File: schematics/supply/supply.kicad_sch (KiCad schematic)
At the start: 14 parts, among them J1 Conn_01x02_Pin, J2 Conn_01x02_Pin, J3 Conn_01x01_Pin, J4 Conn_01x01_Pin

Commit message: Project splited to 2 sub-projects - I want to reduce board production price
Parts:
- removed H1 (x3): MountingHole, MountingHole:MountingHole_2.2mm_M2, symbol Mechanical:MountingHole
- removed J1: Conn_01x02_Pin, Connector_Wire:SolderWire-1.5sqmm_1x02_P6mm_D1.7mm_OD3mm, symbol Connector:Conn_01x02_Pin
- removed J3: Conn_01x01_Pin, Connector_Wire:SolderWire-1.5sqmm_1x01_D1.7mm_OD3.9mm, symbol Connector:Conn_01x01_Pin
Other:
- removed sheet Input power with filter
- removed sheet Standby Supply
- note removed: "Holes on board#2"
- moved on the sheet: J2, J4

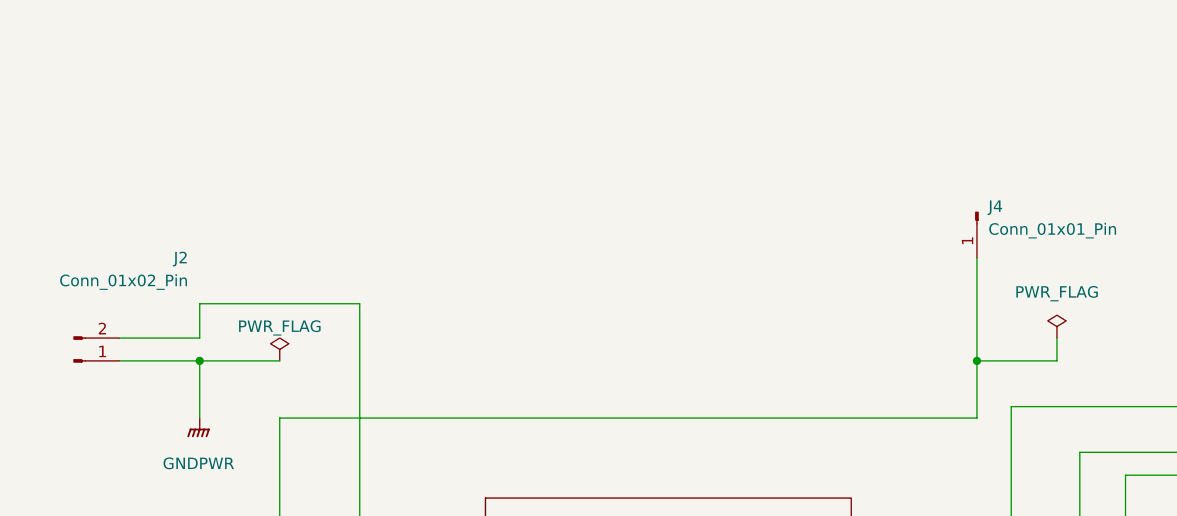
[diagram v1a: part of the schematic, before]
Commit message: UV board size changed to 100x100 to reduce production price
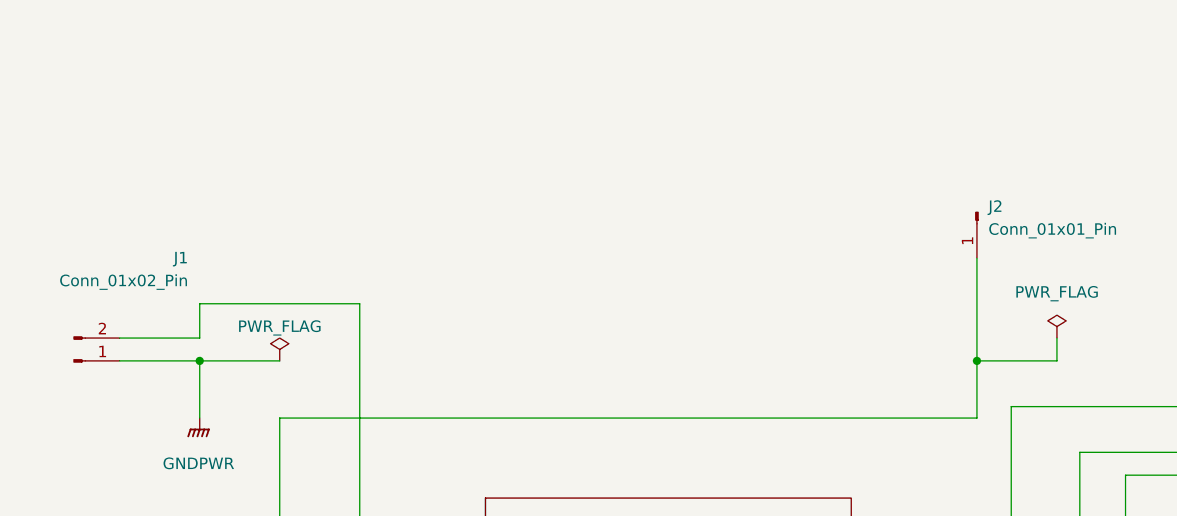
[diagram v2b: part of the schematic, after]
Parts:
- renumbered J2 to J1, J4 to J2
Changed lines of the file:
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@@
   (symbol (lib_id "Connector:Conn_01x01_Pin") (at 157.48 52.07 270) (unit 1)
     (in_bom yes) (on_board yes) (dnp no) (fields_autoplaced)
-    (property "Reference" "J4" (at 158.75 51.435 90)
+    (property "Reference" "J2" (at 158.75 51.435 90)
       (effects (font (size 1.27 1.27)) (justify left))
     )
@@
       (project "supply"
         (path "/1e139717-fcd1-4008-a6ea-4c993845e928"
-          (reference "J4") (unit 1)
+          (reference "J2") (unit 1)
         )
       )
@@
   (symbol (lib_id "Connector:Conn_01x02_Pin") (at 57.15 68.58 0) (mirror x) (unit 1)
     (in_bom yes) (on_board yes) (dnp no)
-    (property "Reference" "J2" (at 69.85 57.15 0)
+    (property "Reference" "J1" (at 69.85 57.15 0)
       (effects (font (size 1.27 1.27)) (justify right))
     )
@@
       (project "supply"
         (path "/1e139717-fcd1-4008-a6ea-4c993845e928"
-          (reference "J2") (unit 1)
+          (reference "J1") (unit 1)
         )
       )

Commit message: Found and fixed issues in schematics.
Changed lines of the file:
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@@
     (stroke (width 0) (type default))
+  )
+  (text_box "Known issues:\n1. Wrong symbol for protection diodes SMAJxx, be carefull with soldering!"
+    (at 314.96 17.78 0) (size 83.82 59.69)
+    (stroke (width 0) (type default))
+    (fill (type none))
+    (effects (font (size 1.27 1.27)) (justify left top))
   )
   (text_box "Startup sequence:\n1. UV board\n1.0 check resistance on 220V connector, OUT_400V connector and STB VCC connector\n1.1 connect 220V\n1.2 check: \n    - OUT_400V is a 310V\n    - PFC EN jumper has 13.7V on one side \n    - STB EN is a HIGH on one side\n    - STB VCC has no power\n    - relay is OFF\n    - LED PFCRDY is ON\n    - LED STBOK is OFF\n1.3 solder PFC EN jumoer\n1.4 check:\n    - OUT_400V is a 400V\n    - PFC EN jumper has 13.7V\n    - STB EN is a LOW on one side\n    - STB VCC has no power\n    - relay is ON\n    - LED PFCRDY is ON\n    - LED STBOK is OFF\n1.5 solder STB EN\n1.6 check:\n    - OUT_400V is a 400V\n    - PFC EN jumper has 13.7V\n    - STB EN is a LOW\n    - STB VCC has 13.7V\n    - relay is ON\n    - LED PFCRDY is ON\n    - LED STBOK is ON\n\n2. UV board & power boards\n2.1 check resistance on +400V connector, PWR OUT connector, 5V connector 3.3V connector and all jumpers\n2.2 flush firmwares\n2.3 connect VV board to power board and connect 220V\n2.4 check:\n    - +400V has 400V\n    - STB VCC has 13.7V\n    - PWR OUT has now power\n    - +5V and 3.3V connectors power\n    - USBx jumper and +5V SYS jumper has 5V on one side\n2.5 insert +5V SYS fuse\n2.6 check:\n    - +5V and 3.3V connectors has no power\n    - USBx jumper has 5V on one side\n    - +5V SYS has 5V\n    - Display is ON\n    - PWR OUT voltage controlled by chips\n    - FAN controlled by termisters and chip\n2.7 solder USB2 & USB3 jumpers\n2.8 check: \n    - usb2 & usb3 works\n    - usb2 & usb3 leds works\n    - display shows usb2 & usb3 voltage and current\n2.9 solder USB1 jumper\n2.10 check \n    - usb1 works\n    - usb1 QC works\n    - usb1 led works\n    - display shows usb1 voltage and current\n"

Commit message: Continue soldering and setting up hardware
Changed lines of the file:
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@@
     (stroke (width 0) (type default))
   )
-  (text_box "Known issues:\n1. Wrong symbol for protection diodes SMAJxx, be carefull with soldering!"
+  (text_box "Known issues:\n1. Wrong symbol for protection diodes SMAJxx, be carefull with soldering!\n2. Power output starts without +5VSYS"
     (at 314.96 17.78 0) (size 83.82 59.69)
     (stroke (width 0) (type default))

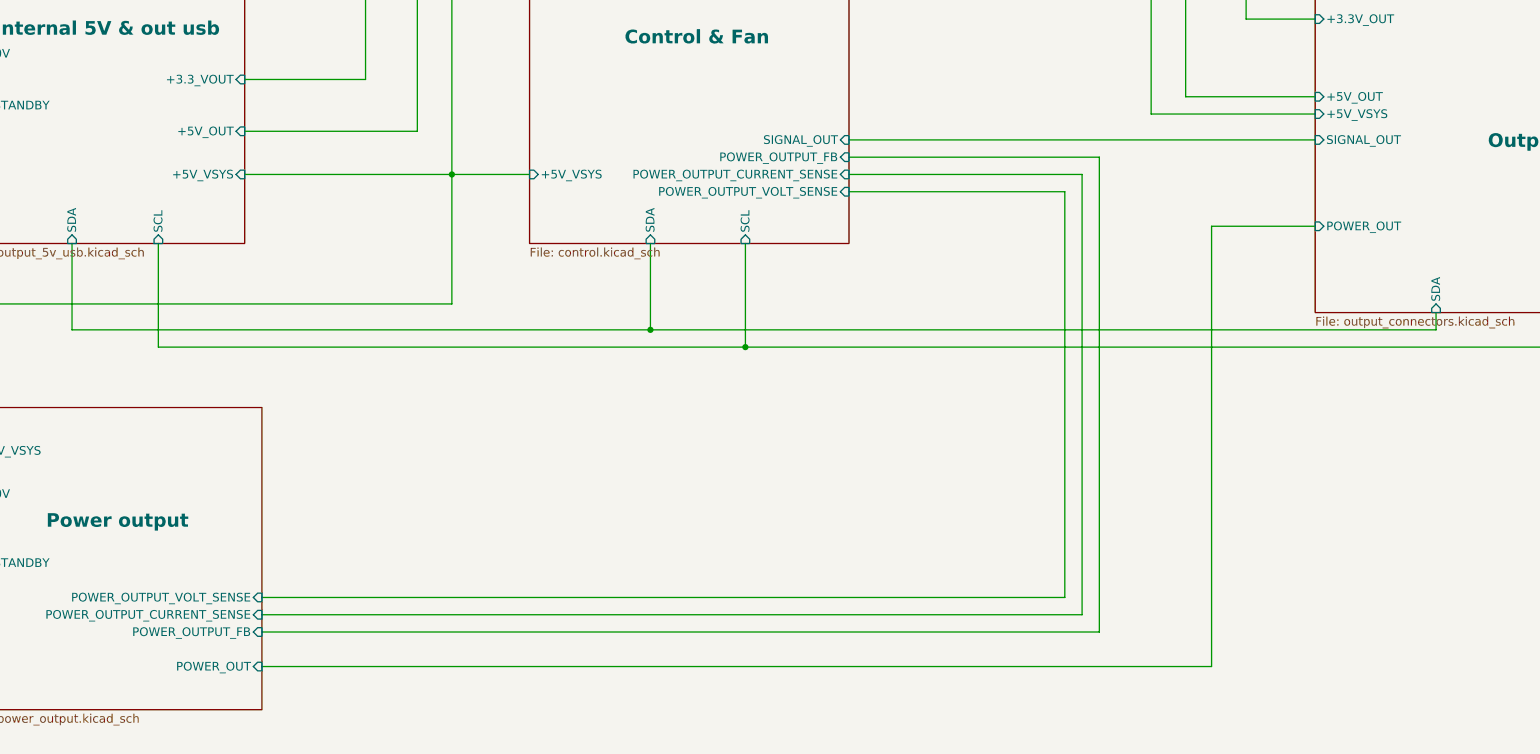
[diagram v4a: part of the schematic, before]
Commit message: supply board - power controllers changed; PWM logic changed
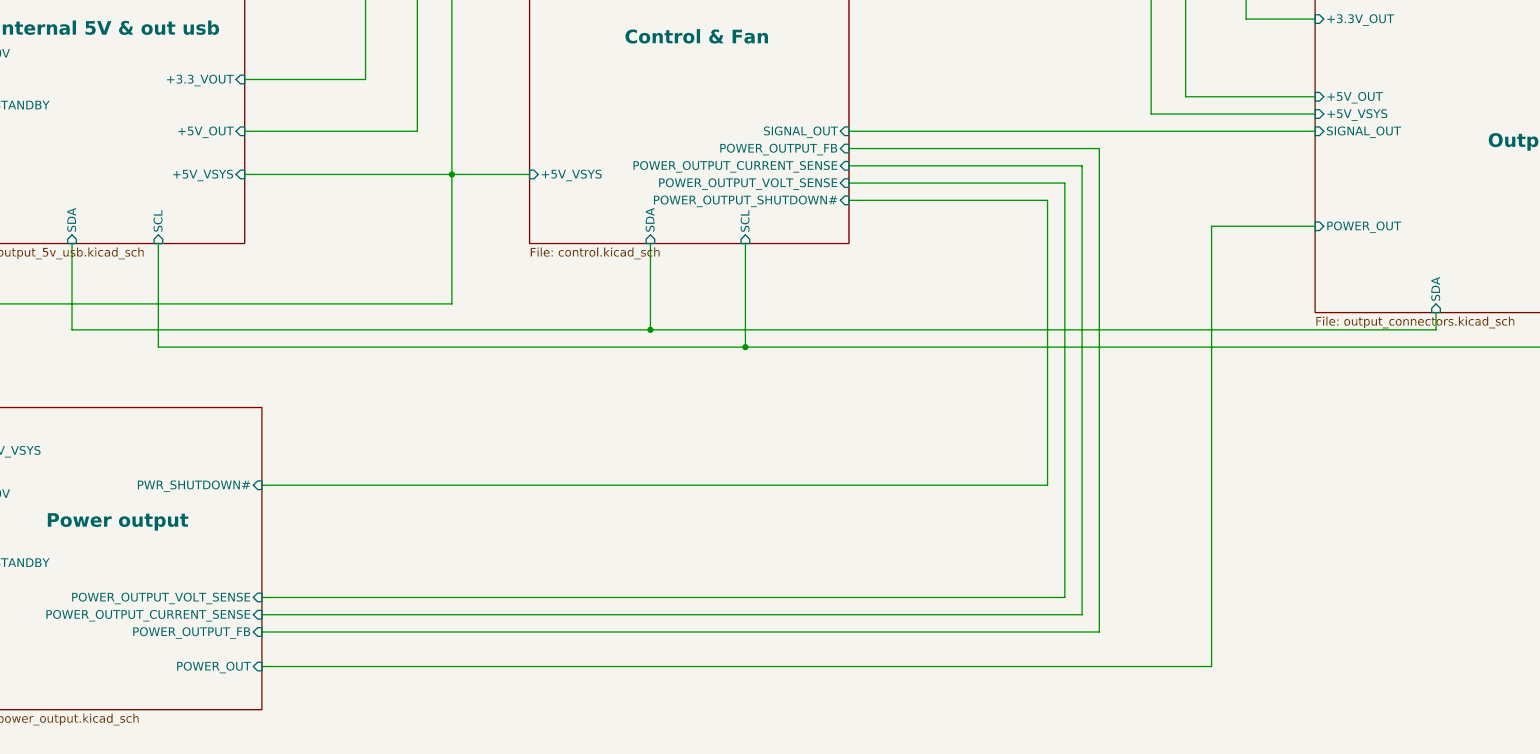
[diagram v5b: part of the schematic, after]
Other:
- sheet Control & Fan ports: added POWER_OUTPUT_SHUTDOWN#; removed none
- sheet Power output ports: added PWR_SHUTDOWN#; removed none
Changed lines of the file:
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@@
     (stroke (width 0) (type default))
   )
-  (wire (pts (xy 269.24 111.76) (xy 232.41 111.76))
+  (wire (pts (xy 269.24 110.49) (xy 232.41 110.49))
     (stroke (width 0) (type default))
   )
@@
     (stroke (width 0) (type default))
   )
+  (wire (pts (xy 261.62 160.02) (xy 146.05 160.02))
+    (stroke (width 0) (type default))
+  )
   (wire (pts (xy 166.37 68.58) (xy 157.48 68.58))
     (stroke (width 0) (type default))
   )
-  (wire (pts (xy 269.24 181.61) (xy 269.24 111.76))
+  (wire (pts (xy 269.24 181.61) (xy 269.24 110.49))
+    (stroke (width 0) (type default))
+  )
+  (wire (pts (xy 232.41 107.95) (xy 300.99 107.95))
     (stroke (width 0) (type default))
   )
@@
     (stroke (width 0) (type default))
   )
-  (wire (pts (xy 266.7 114.3) (xy 266.7 179.07))
+  (wire (pts (xy 266.7 113.03) (xy 266.7 179.07))
     (stroke (width 0) (type default))
   )
@@
     (stroke (width 0) (type default))
   )
-  (wire (pts (xy 232.41 109.22) (xy 300.99 109.22))
-    (stroke (width 0) (type default))
-  )
   (wire (pts (xy 71.12 68.58) (xy 80.01 68.58))
     (stroke (width 0) (type default))
@@
     (stroke (width 0) (type default))
   )
+  (wire (pts (xy 261.62 118.11) (xy 261.62 160.02))
+    (stroke (width 0) (type default))
+  )
   (wire (pts (xy 88.9 96.52) (xy 88.9 62.23))
     (stroke (width 0) (type default))
@@
     (stroke (width 0) (type default))
   )
-  (wire (pts (xy 264.16 116.84) (xy 232.41 116.84))
+  (wire (pts (xy 264.16 115.57) (xy 232.41 115.57))
     (stroke (width 0) (type default))
   )
@@
     (stroke (width 0) (type default))
   )
-  (wire (pts (xy 264.16 176.53) (xy 264.16 116.84))
-    (stroke (width 0) (type default))
-  )
-  (wire (pts (xy 232.41 114.3) (xy 266.7 114.3))
+  (wire (pts (xy 264.16 176.53) (xy 264.16 115.57))
+    (stroke (width 0) (type default))
+  )
+  (wire (pts (xy 232.41 113.03) (xy 266.7 113.03))
     (stroke (width 0) (type default))
   )
@@
   )
   (wire (pts (xy 161.29 100.33) (xy 161.29 73.66))
+    (stroke (width 0) (type default))
+  )
+  (wire (pts (xy 232.41 118.11) (xy 261.62 118.11))
     (stroke (width 0) (type default))
   )
@@
       (effects (font (size 1.27 1.27)) (justify left))
     )
-    (pin "SIGNAL_OUT" input (at 300.99 109.22 180)
+    (pin "SIGNAL_OUT" input (at 300.99 107.95 180)
       (effects (font (size 1.27 1.27)) (justify left))
     )
@@
       (effects (font (size 1.27 1.27)) (justify left))
     )
+    (pin "PWR_SHUTDOWN#" input (at 146.05 160.02 0)
+      (effects (font (size 1.27 1.27)) (justify right))
+    )
     (instances
       (project "supply"
@@
       (effects (font (size 1.27 1.27)) (justify left))
     )
-    (pin "SIGNAL_OUT" input (at 232.41 109.22 0)
-      (effects (font (size 1.27 1.27)) (justify right))
-    )
-    (pin "POWER_OUTPUT_FB" input (at 232.41 111.76 0)
-      (effects (font (size 1.27 1.27)) (justify right))
-    )
-    (pin "POWER_OUTPUT_CURRENT_SENSE" input (at 232.41 114.3 0)
-      (effects (font (size 1.27 1.27)) (justify right))
-    )
-    (pin "POWER_OUTPUT_VOLT_SENSE" input (at 232.41 116.84 0)
+    (pin "SIGNAL_OUT" input (at 232.41 107.95 0)
+      (effects (font (size 1.27 1.27)) (justify right))
+    )
+    (pin "POWER_OUTPUT_FB" input (at 232.41 110.49 0)
+      (effects (font (size 1.27 1.27)) (justify right))
+    )
+    (pin "POWER_OUTPUT_CURRENT_SENSE" input (at 232.41 113.03 0)
+      (effects (font (size 1.27 1.27)) (justify right))
+    )
+    (pin "POWER_OUTPUT_VOLT_SENSE" input (at 232.41 115.57 0)
       (effects (font (size 1.27 1.27)) (justify right))
     )
@@
       (effects (font (size 1.27 1.27)) (justify left))
     )
-    (instances
+    (pin "POWER_OUTPUT_SHUTDOWN#" input (at 232.41 118.11 0)
+      (effects (font (size 1.27 1.27)) (justify right))
+    )
+    (instances
